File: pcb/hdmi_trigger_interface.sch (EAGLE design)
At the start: 2 parts

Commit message: work on hdmi integration into basler trigger circuitry
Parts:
- added CAMERA1, CAMERA2: 87438-06, con-molex:87438-06
- added LINE_1_1, LINE_1_2, LINE_1_3, LINE_1_4, LINE_2_1, LINE_2_2, LINE_2_3, LINE_2_4, TP_GND: TPTP16R, testpad:TPTP16R
- added P1, P2: 10029449-001RLF, 10029449-001RLF:10029449-001RLF
- added R1, R10, R11, R12, R13, R14, R15, R16, R17, R18, R19, R2, R20, R21, R22, R23, R24, R25, R26, R3, R4, R7, R8, R9: (no value), rcl:R-US_R0603
- added U1, U2: TPD12S016PWR, TPD12S016:TPD12S016PWR
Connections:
- new net 3V3: R11.2, R12.2, R13.2, R14.2, R15.2, R16.2, R17.2, R18.2, U$1G$2.+V, U$1G$3.+V
- new net CLK1_N: P1.12, U$1G$2.143, U1.CLK-
- new net CLK1_P: P1.10, U$1G$2.144, U1.CLK+
- new net CLK2_N: P2.12, U$1G$3.120
- new net CLK2_P: P2.10, U$1G$3.121
- new net D01_N: P1.9, U$1G$2.141, U1.D0-
- new net D01_P: P1.7, U$1G$2.142, U1.D0+
- new net D02_N: P2.9, U$1G$3.118
- new net D02_P: P2.7, U$1G$3.119
- new net D11_N: P1.6, U$1G$2.139, U1.D1-
- new net D11_P: P1.4, U$1G$2.140, U1.D1+
- new net D12_N: P2.6, U$1G$3.116
- new net D12_P: P2.4, U$1G$3.117
- new net D21_N: P1.3, U$1G$2.137, U1.D2-
- new net D21_P: P1.1, U$1G$2.138, U1.D2+
- new net D22_N: P2.3, U$1G$3.114
- new net D22_P: P2.1, U$1G$3.115
- new net GND: CAMERA1-5.S, CAMERA1-6.S, CAMERA2-5.S, CAMERA2-6.S, P1.11, P1.17, P1.2, P1.5, P1.8, P2.11, P2.17, P2.2, P2.5, P2.8, R19.1, R20.1, R21.1, R22.1, R23.1, R24.1, R25.1, R26.1, TP_GND.TP
- new net GND@1: U$1G$2.GND@1, U$1G$2.GND@2, U$1G$3.GND@1, U$1G$3.GND@2
- new net HP1: P1.19, U1.HPD_B-
- new net HP2: P2.19
- new net LINE_1_1: LINE_1_1.TP, R14.1, R22.2, R4.1
- new net LINE_1_2: LINE_1_2.TP, R13.1, R21.2, R3.1
- new net LINE_1_3: LINE_1_3.TP, R12.1, R2.1, R20.2
- new net LINE_1_4: LINE_1_4.TP, R1.1, R11.1, R19.2
- new net LINE_2_1: LINE_2_1.TP, R10.1, R18.1, R26.2
- new net LINE_2_2: LINE_2_2.TP, R17.1, R25.2, R9.1
- new net LINE_2_3: LINE_2_3.TP, R16.1, R24.2, R8.1
- new net LINE_2_4: LINE_2_4.TP, R15.1, R23.2, R7.1
- new net N$1: U1.5V_OUT
- new net N$10: CAMERA2-2.S, R8.2
- new net N$11: CAMERA2-3.S, R9.2
- new net N$12: CAMERA2-4.S, R10.2
- new net N$14: U1.GND
- new net N$19: U1.GND_3
- new net N$22: P1.18
- new net N$3: U1.VCCA
- new net N$39: P2.18
- new net N$5: CAMERA1-1.S, R1.2
- new net N$6: CAMERA1-2.S, R2.2
- new net N$7: CAMERA1-3.S, R3.2
- new net N$8: CAMERA1-4.S, R4.2
- new net N$9: CAMERA2-1.S, R7.2
- new net SCL1: P1.15, U1.SCL_B
- new net SCL1_M: U$1G$2.1, U1.SCL_A
- new net SCL2: P2.15, U$1G$3.112
- new net SDA1: P1.16, U1.SDA_B
- new net SDA1_M: U$1G$2.2, U1.SDA_A
- new net SDA2: P2.16, U$1G$3.111

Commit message: almost done with routing
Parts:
- added C1: 0.1uF, rcl:C-USC0603
- added C2: 1uF, rcl:C-USC0603
- added R5, R6: 3k, rcl:R-US_R0603
- added Y1: SI514, lupa300-components:SI514
- renumbered P1 to HDMI_1, P2 to HDMI_2
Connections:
- removed net GND@1: U$1G$2.GND@1, U$1G$2.GND@2, U$1G$3.GND@1, U$1G$3.GND@2
- removed net N$1: U1.5V_OUT
- removed net N$14: U1.GND
- removed net N$19: U1.GND_3
- removed net N$22: HDMI_1.18
- removed net N$3: U1.VCCA
- removed net N$39: HDMI_2.18
- new net 5V: U$1G$2.RAW, U$1G$3.RAW, U1.VCC5V, U2.VCC5V
- new net 5VHDMI1: HDMI_1.18, U1.5V_OUT
- new net 5VHDMI2: HDMI_2.18, U2.5V_OUT
- new net CTHPD1: U1.CT_HPD
- new net CTHPD2: U2.CT_HPD
- new net HP1_M: U1.HPD_A-, U1.LS_OE
- new net HP2_M: U2.HPD_A-, U2.LS_OE
- new net PROG_CLK: U$1G$2.51, Y1.CLK
- new net SCL2_M: U$1G$3.112, U2.SCL_A
- new net SCL_C: R5.1, U$1G$2.23, Y1.SCL
- new net SDA2_M: U$1G$3.111, U2.SDA_A
- new net SDA_C: R6.1, U$1G$2.24, Y1.SDA
- net 3V3: now also C1.1, C2.1, R5.2, R6.2, U1.VCCA, U2.VCCA, Y1.VDD
- net CLK2_N: now also U2.CLK-
- net CLK2_P: now also U2.CLK+
- net D02_N: now also U2.D0-
- net D02_P: now also U2.D0+
- net D12_N: now also U2.D1-
- net D12_P: now also U2.D1+
- net D22_N: now also U2.D2-
- net D22_P: now also U2.D2+
- net GND: now also C1.2, C2.2, U$1G$2.GND@1, U$1G$2.GND@2, U$1G$3.GND@1, U$1G$3.GND@2, U$1G$3.GND@3, U1.GND, U1.GND_2, U1.GND_3, U2.GND, U2.GND_2, U2.GND_3, Y1.GND
- net HP2: now also U2.HPD_B-
- net LINE_1_1: now also U$1G$2.12; no longer LINE_1_1.TP
- net LINE_1_2: now also U$1G$2.11; no longer LINE_1_2.TP
- net LINE_1_3: now also U$1G$2.15; no longer LINE_1_3.TP
- net LINE_1_4: now also U$1G$2.14; no longer LINE_1_4.TP
- net LINE_2_1: now also U$1G$2.17; no longer LINE_2_1.TP
- net LINE_2_2: now also U$1G$2.16; no longer LINE_2_2.TP
- net LINE_2_3: now also U$1G$2.22; no longer LINE_2_3.TP
- net LINE_2_4: now also U$1G$2.21; no longer LINE_2_4.TP
- net N$10: now also LINE_2_3.TP
- net N$11: now also LINE_2_2.TP
- net N$12: now also LINE_2_1.TP
- net N$5: now also LINE_1_4.TP
- net N$6: now also LINE_1_3.TP
- net N$7: now also LINE_1_2.TP
- net N$8: now also LINE_1_1.TP
- net N$9: now also LINE_2_4.TP
- net SCL2: now also U2.SCL_B; no longer U$1G$3.112
- net SDA2: now also U2.SDA_B; no longer U$1G$3.111

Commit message: board layout 90% done, need parts list then will order
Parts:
- added C10, C3, C4, C5, C6, C7, C8, C9: 1uF, rcl:C-USC0603
- added R27, R28, R29, R30: 10k, rcl:R-US_R0603
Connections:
- new net N$13: C9.1, HDMI_1.P$1, HDMI_1.P$2, HDMI_1.P$3, HDMI_1.P$4, R29.1
- new net N$14: C10.1, HDMI_2.P$1, HDMI_2.P$2, HDMI_2.P$3, HDMI_2.P$4, R30.1
- net 3V3: now also C7.1, C8.1, R27.1, R28.1
- net 5V: now also C3.1, C5.1
- net 5VHDMI1: now also C4.1
- net 5VHDMI2: now also C6.1
- net CTHPD1: now also R27.2, U$1G$2.7
- net CTHPD2: now also R28.2, U$1G$3.102
- net GND: now also C10.2, C3.2, C4.2, C5.2, C6.2, C7.2, C8.2, C9.2, R29.2, R30.2

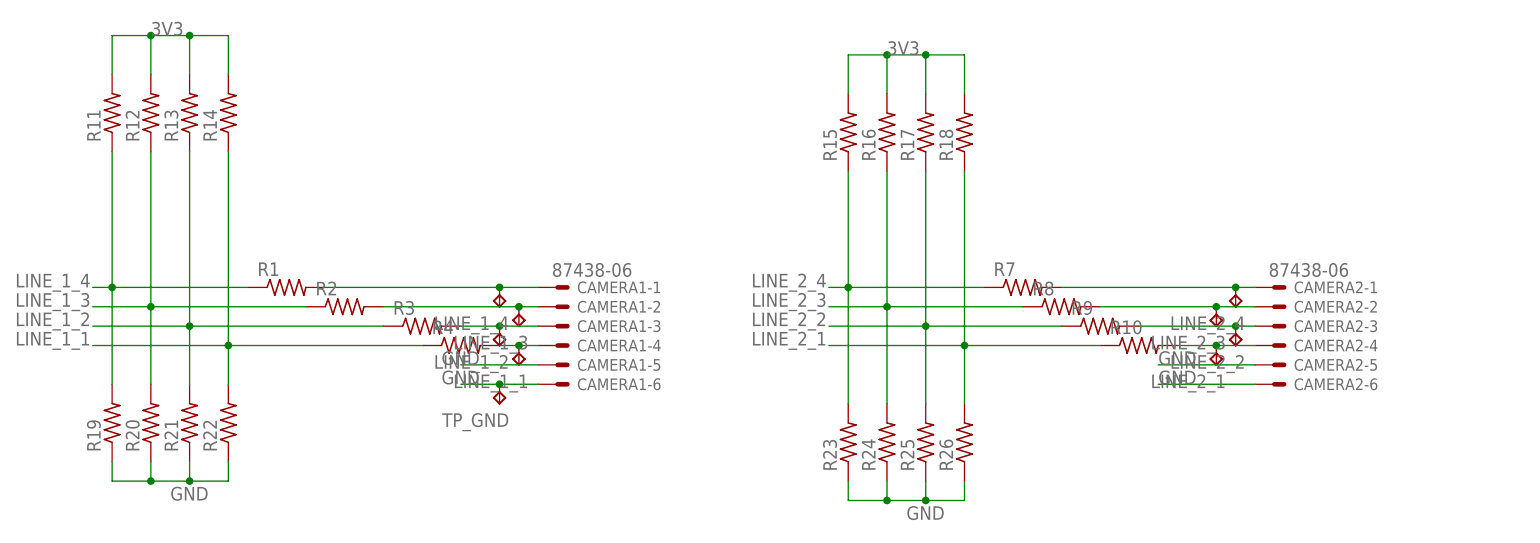
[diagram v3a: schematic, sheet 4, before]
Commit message: added images from manufacturing render and gerbers sent to pcbway
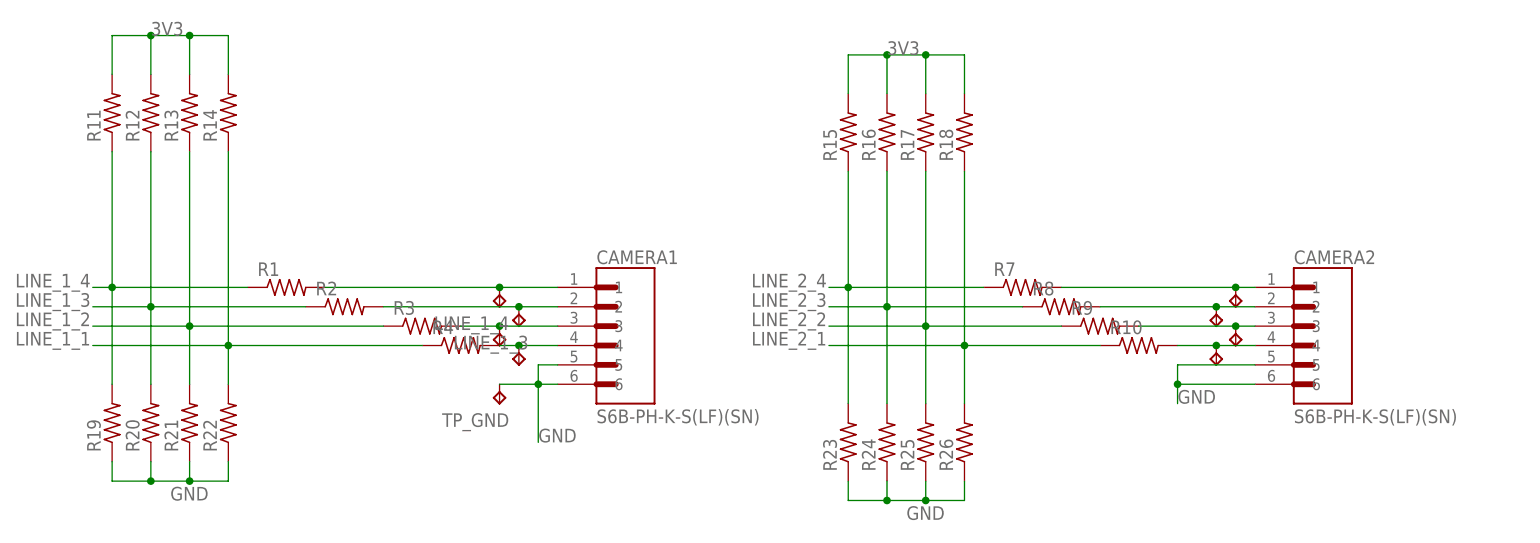
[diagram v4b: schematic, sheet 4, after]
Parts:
- CAMERA1, CAMERA2: value 87438-06 -> S6B-PH-K-S(LF)(SN); device con-molex:87438-06 -> S6B-PH-K-S_LF__SN_:S6B-PH-K-S(LF)(SN)
- LINE_2_1, LINE_4: value TPTP16R -> LINE_1
- LINE_2_2: value TPTP16R -> LINE_2
- LINE_2_3: value TPTP16R -> LINE_3
- renumbered LINE_2_4 to LINE_4
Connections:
- net GND: now also CAMERA1.5, CAMERA1.6, CAMERA2.5, CAMERA2.6; no longer CAMERA1-5.S, CAMERA1-6.S, CAMERA2-5.S, CAMERA2-6.S
- net N$10: now also CAMERA2.2; no longer CAMERA2-2.S
- net N$11: now also CAMERA2.3; no longer CAMERA2-3.S
- net N$12: now also CAMERA2.4; no longer CAMERA2-4.S
- net N$5: now also CAMERA1.1; no longer CAMERA1-1.S
- net N$6: now also CAMERA1.2; no longer CAMERA1-2.S
- net N$7: now also CAMERA1.3; no longer CAMERA1-3.S
- net N$8: now also CAMERA1.4; no longer CAMERA1-4.S
- net N$9: now also CAMERA2.1; no longer CAMERA2-1.S

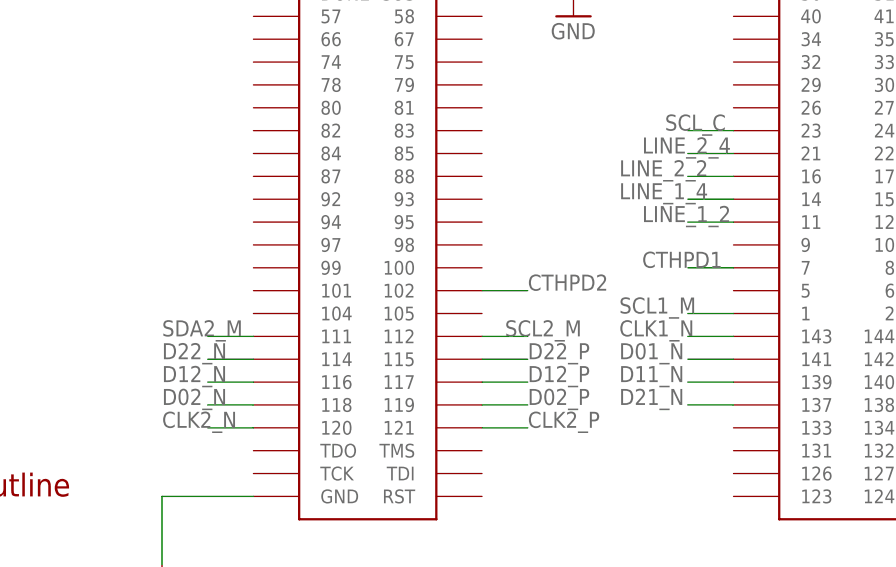
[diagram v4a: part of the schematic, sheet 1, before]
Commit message: length tuning and routing done, need final review then ready to order
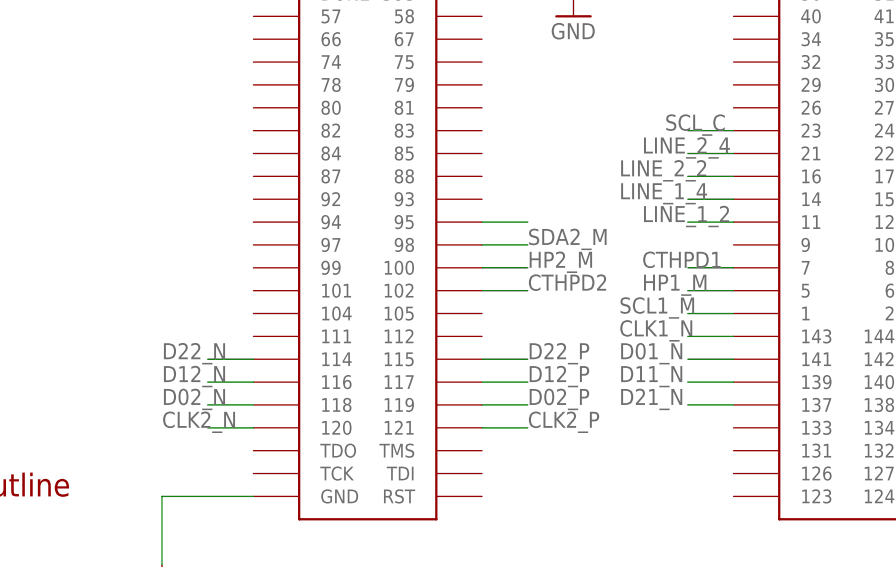
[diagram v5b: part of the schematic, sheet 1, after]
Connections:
- net HP1_M: now also U$1G$2.5
- net HP2_M: now also U$1G$3.100
- net SCL2_M: now also U$1G$3.95; no longer U$1G$3.112
- net SDA2_M: now also U$1G$3.98; no longer U$1G$3.111
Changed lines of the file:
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@@
 <net name="SDA2_M" class="0">
 <segment>
-<pinref part="U$1" gate="G$3" pin="111"/>
-<wire x1="53.34" y1="25.4" x2="48.26" y2="25.4" width="0.1524" layer="91"/>
-<label x="43.18" y="25.4" size="1.778" layer="95"/>
+<pinref part="U$1" gate="G$3" pin="98"/>
+<wire x1="78.74" y1="35.56" x2="83.82" y2="35.56" width="0.1524" layer="91"/>
+<label x="83.82" y="35.56" size="1.778" layer="95"/>
 </segment>
 </net>
 <net name="SCL2_M" class="0">
 <segment>
-<pinref part="U$1" gate="G$3" pin="112"/>
-<wire x1="78.74" y1="25.4" x2="83.82" y2="25.4" width="0.1524" layer="91"/>
-<label x="81.28" y="25.4" size="1.778" layer="95"/>
+<pinref part="U$1" gate="G$3" pin="95"/>
+<wire x1="78.74" y1="38.1" x2="83.82" y2="38.1" width="0.1524" layer="91"/>
 </segment>
 </net>
@@
 </segment>
 </net>
+<net name="HP2_M" class="0">
+<segment>
+<pinref part="U$1" gate="G$3" pin="100"/>
+<wire x1="78.74" y1="33.02" x2="83.82" y2="33.02" width="0.1524" layer="91"/>
+<label x="83.82" y="33.02" size="1.778" layer="95"/>
+</segment>
+</net>
+<net name="HP1_M" class="0">
+<segment>
+<pinref part="U$1" gate="G$2" pin="5"/>
+<wire x1="106.68" y1="30.48" x2="101.6" y2="30.48" width="0.1524" layer="91"/>
+<label x="96.52" y="30.48" size="1.778" layer="95"/>
+</segment>
+</net>

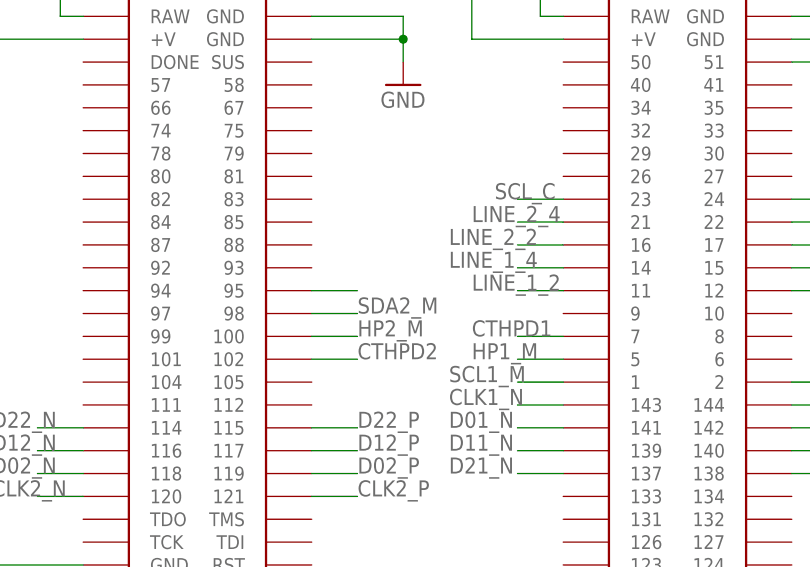
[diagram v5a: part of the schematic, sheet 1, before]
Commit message: ripped up old diff pairs, ready to route new 8/8 lines
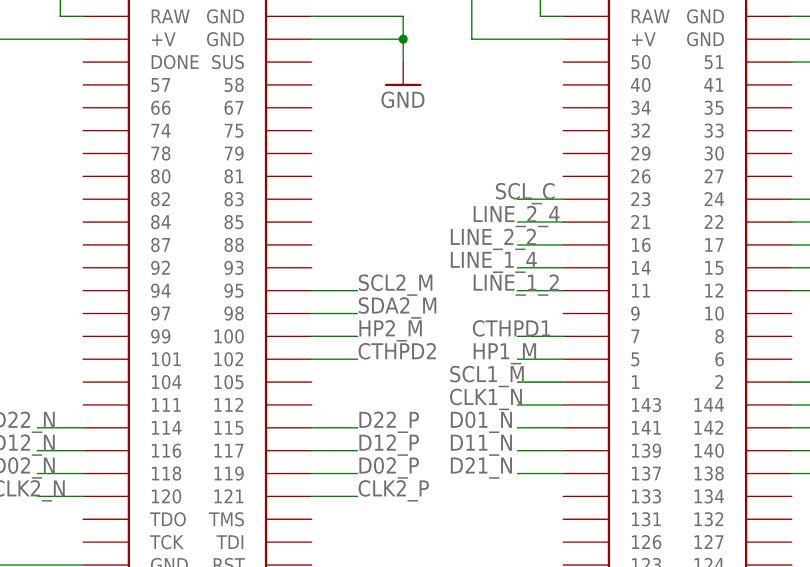
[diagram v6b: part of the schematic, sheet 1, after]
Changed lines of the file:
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@@
 <?xml version="1.0" encoding="utf-8"?>
 <!DOCTYPE eagle SYSTEM "eagle.dtd">
-<eagle version="9.3.0">
+<eagle version="9.3.1">
 <drawing>
 <settings>
@@
 <layer number="54" name="bGND_GNDA" color="7" fill="1" visible="no" active="no"/>
 <layer number="56" name="wert" color="7" fill="1" visible="no" active="no"/>
+<layer number="57" name="tCAD" color="7" fill="1" visible="no" active="no"/>
+<layer number="59" name="tCarbon" color="7" fill="1" visible="no" active="no"/>
+<layer number="60" name="bCarbon" color="7" fill="1" visible="no" active="no"/>
 <layer number="88" name="SimResults" color="9" fill="1" visible="yes" active="yes"/>
 <layer number="89" name="SimProbes" color="9" fill="1" visible="yes" active="yes"/>
@@
 <layer number="106" name="bPlate" color="7" fill="1" visible="yes" active="yes"/>
 <layer number="107" name="Crop" color="7" fill="1" visible="yes" active="yes"/>
+<layer number="108" name="fp8" color="7" fill="1" visible="no" active="yes"/>
+<layer number="109" name="fp9" color="7" fill="1" visible="no" active="yes"/>
+<layer number="110" name="fp0" color="7" fill="1" visible="no" active="yes"/>
 <layer number="111" name="tGTest" color="7" fill="1" visible="yes" active="yes"/>
 <layer number="112" name="bGTest" color="7" fill="1" visible="yes" active="yes"/>
+<layer number="113" name="ReferenceLS" color="7" fill="1" visible="no" active="no"/>
 <layer number="116" name="Patch_BOT" color="7" fill="1" visible="yes" active="yes"/>
+<layer number="118" name="Rect_Pads" color="7" fill="1" visible="no" active="no"/>
 <layer number="121" name="tsilk" color="7" fill="1" visible="yes" active="yes"/>
 <layer number="122" name="bSilk" color="7" fill="1" visible="yes" active="yes"/>
+<layer number="123" name="tTestmark" color="7" fill="1" visible="no" active="yes"/>
+<layer number="124" name="bTestmark" color="7" fill="1" visible="no" active="yes"/>
 <layer number="125" name="_tNames" color="7" fill="1" visible="yes" active="yes"/>
+<layer number="126" name="_bNames" color="7" fill="1" visible="no" active="yes"/>
+<layer number="127" name="_tValues" color="7" fill="1" visible="no" active="yes"/>
+<layer number="128" name="_bValues" color="7" fill="1" visible="no" active="yes"/>
+<layer number="129" name="Mask" color="7" fill="1" visible="yes" active="yes"/>
+<layer number="131" name="tAdjust" color="7" fill="1" visible="no" active="yes"/>
+<layer number="132" name="bAdjust" color="7" fill="1" visible="no" active="yes"/>
 <layer number="144" name="Drill_legend" color="7" fill="1" visible="yes" active="yes"/>
 <layer number="150" name="Notes" color="7" fill="1" visible="yes" active="yes"/>
 <layer number="151" name="HeatSink" color="7" fill="1" visible="yes" active="yes"/>
+<layer number="152" name="_bDocu" color="7" fill="1" visible="no" active="yes"/>
+<layer number="153" name="FabDoc1" color="6" fill="1" visible="no" active="no"/>
+<layer number="154" name="FabDoc2" color="2" fill="1" visible="no" active="no"/>
+<layer number="155" name="FabDoc3" color="7" fill="15" visible="no" active="no"/>
 <layer number="199" name="Contour" color="7" fill="1" visible="yes" active="yes"/>
 <layer number="200" name="200bmp" color="7" fill="1" visible="yes" active="yes"/>
@@
 <layer number="223" name="223bmp" color="7" fill="1" visible="yes" active="yes"/>
 <layer number="224" name="224bmp" color="7" fill="1" visible="yes" active="yes"/>
+<layer number="225" name="225bmp" color="7" fill="1" visible="yes" active="yes"/>
+<layer number="226" name="226bmp" color="7" fill="1" visible="yes" active="yes"/>
+<layer number="227" name="227bmp" color="7" fill="1" visible="yes" active="yes"/>
+<layer number="228" name="228bmp" color="7" fill="1" visible="yes" active="yes"/>
+<layer number="229" name="229bmp" color="7" fill="1" visible="yes" active="yes"/>
+<layer number="230" name="230bmp" color="7" fill="1" visible="yes" active="yes"/>
+<layer number="231" name="Eagle3D_PG1" color="7" fill="1" visible="no" active="no"/>
+<layer number="232" name="Eagle3D_PG2" color="7" fill="1" visible="no" active="no"/>
+<layer number="233" name="Eagle3D_PG3" color="7" fill="1" visible="no" active="no"/>
+<layer number="248" name="Housing" color="7" fill="1" visible="no" active="yes"/>
+<layer number="249" name="Edge" color="7" fill="1" visible="no" active="yes"/>
 <layer number="250" name="Descript" color="7" fill="1" visible="yes" active="yes"/>
 <layer number="251" name="SMDround" color="7" fill="1" visible="yes" active="yes"/>
 <layer number="254" name="cooling" color="7" fill="1" visible="yes" active="yes"/>
+<layer number="255" name="routoute" color="7" fill="1" visible="yes" active="yes"/>
 </layers>
 <schematic xreflabel="%F%N/%S.%C%R" xrefpart="/%S.%C%R">
@@
 <pinref part="U$1" gate="G$3" pin="95"/>
 <wire x1="78.74" y1="38.1" x2="83.82" y2="38.1" width="0.1524" layer="91"/>
-</segment>
-</net>
+<label x="83.82" y="38.1" size="1.778" layer="95"/>
+</segment>
+</net>

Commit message: more routing
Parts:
- added X1, X2: 87438-06, con-molex:87438-06
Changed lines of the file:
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@@
 <part name="CAMERA1" library="S6B-PH-K-S_LF__SN_" deviceset="S6B-PH-K-S(LF)(SN)" device=""/>
 <part name="CAMERA2" library="S6B-PH-K-S_LF__SN_" deviceset="S6B-PH-K-S(LF)(SN)" device=""/>
+<part name="X1" library="con-molex" library_urn="urn:adsk.eagle:library:165" deviceset="87438-06" device="" package3d_urn="urn:adsk.eagle:package:8078913/1"/>
+<part name="X2" library="con-molex" library_urn="urn:adsk.eagle:library:165" deviceset="87438-06" device="" package3d_urn="urn:adsk.eagle:package:8078913/1"/>
 </parts>
 <sheets>
@@
 <attribute name="VALUE" x="177.8" y="22.8446" size="1.780159375" layer="96"/>
 </instance>
+<instance part="X1" gate="-1" x="86.36" y="68.58" smashed="yes">
+<attribute name="NAME" x="88.9" y="67.818" size="1.524" layer="95"/>
+<attribute name="VALUE" x="85.598" y="69.977" size="1.778" layer="96"/>
+</instance>
+<instance part="X1" gate="-2" x="86.36" y="66.04" smashed="yes">
+<attribute name="NAME" x="88.9" y="65.278" size="1.524" layer="95"/>
+</instance>
+<instance part="X1" gate="-3" x="86.36" y="63.5" smashed="yes">
+<attribute name="NAME" x="88.9" y="62.738" size="1.524" layer="95"/>
+</instance>
+<instance part="X1" gate="-4" x="86.36" y="60.96" smashed="yes">
+<attribute name="NAME" x="88.9" y="60.198" size="1.524" layer="95"/>
+</instance>
+<instance part="X1" gate="-5" x="86.36" y="58.42" smashed="yes">
+<attribute name="NAME" x="88.9" y="57.658" size="1.524" layer="95"/>
+</instance>
+<instance part="X1" gate="-6" x="86.36" y="55.88" smashed="yes">
+<attribute name="NAME" x="88.9" y="55.118" size="1.524" layer="95"/>
+</instance>
+<instance part="X2" gate="-1" x="180.34" y="68.58" smashed="yes">
+<attribute name="NAME" x="182.88" y="67.818" size="1.524" layer="95"/>
+<attribute name="VALUE" x="179.578" y="69.977" size="1.778" layer="96"/>
+</instance>
+<instance part="X2" gate="-2" x="180.34" y="66.04" smashed="yes">
+<attribute name="NAME" x="182.88" y="65.278" size="1.524" layer="95"/>
+</instance>
+<instance part="X2" gate="-3" x="180.34" y="63.5" smashed="yes">
+<attribute name="NAME" x="182.88" y="62.738" size="1.524" layer="95"/>
+</instance>
+<instance part="X2" gate="-4" x="180.34" y="60.96" smashed="yes">
+<attribute name="NAME" x="182.88" y="60.198" size="1.524" layer="95"/>
+</instance>
+<instance part="X2" gate="-5" x="180.34" y="58.42" smashed="yes">
+<attribute name="NAME" x="182.88" y="57.658" size="1.524" layer="95"/>
+</instance>
+<instance part="X2" gate="-6" x="180.34" y="55.88" smashed="yes">
+<attribute name="NAME" x="182.88" y="55.118" size="1.524" layer="95"/>
+</instance>
 </instances>
